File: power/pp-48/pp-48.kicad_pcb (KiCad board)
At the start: 4 copper layers, 106 x 72 mm, 218 parts, among them J1 XT90PW-M, J101 NODE 19V, J102 FRONT PANEL, J103 AUX, J2 CTRL IN, J201 NODE 19V, J202 FRONT PANEL, J203 AUX, J3 CTRL OUT, J4 12V AUX OUT, J5 SWD, Q1 2N7002, Q101 BSC070N10NS5, Q102 2N7002, Q103 2N7002, Q104 2N7002, Q105 2N7002, Q106 2N7002, Q107 2N7002, Q108 2N7002, Q109 2N7002, Q2 BSC040N10NS5, Q201 BSC070N10NS5, Q202 2N7002, Q203 2N7002, Q204 2N7002, Q205 2N7002, Q206 2N7002, Q207 2N7002, Q208 2N7002, Q209 2N7002, Q3 BSC040N10NS5, Q4 2N7002, Q6 2N7002, U1 LM5164DDA, U101 LM5069MM-2, U102 INA238AIDGSR, U103 74LVC1G74, U104 ADC121C027CIMK, U105 TCA9535PWR, U106 TLP176AM, U107 TLP176AM, U108 TLP291, U110 74LVC1G74, U2 URB4812YMD-6WR3, U201 LM5069MM-2, U202 INA238AIDGSR, U203 74LVC1G74, U204 ADC121C027CIMK, U205 TCA9535PWR, U206 TLP176AM, U207 TLP176AM, U208 TLP291, U210 74LVC1G74, U3 STM32G070CBT6, U4 ISO1640BD, U5 ISO7721D, U6 TCA9548APWR, U7 LM5069MM-1, U8 INA238AIDGSR, Y1 8MHz

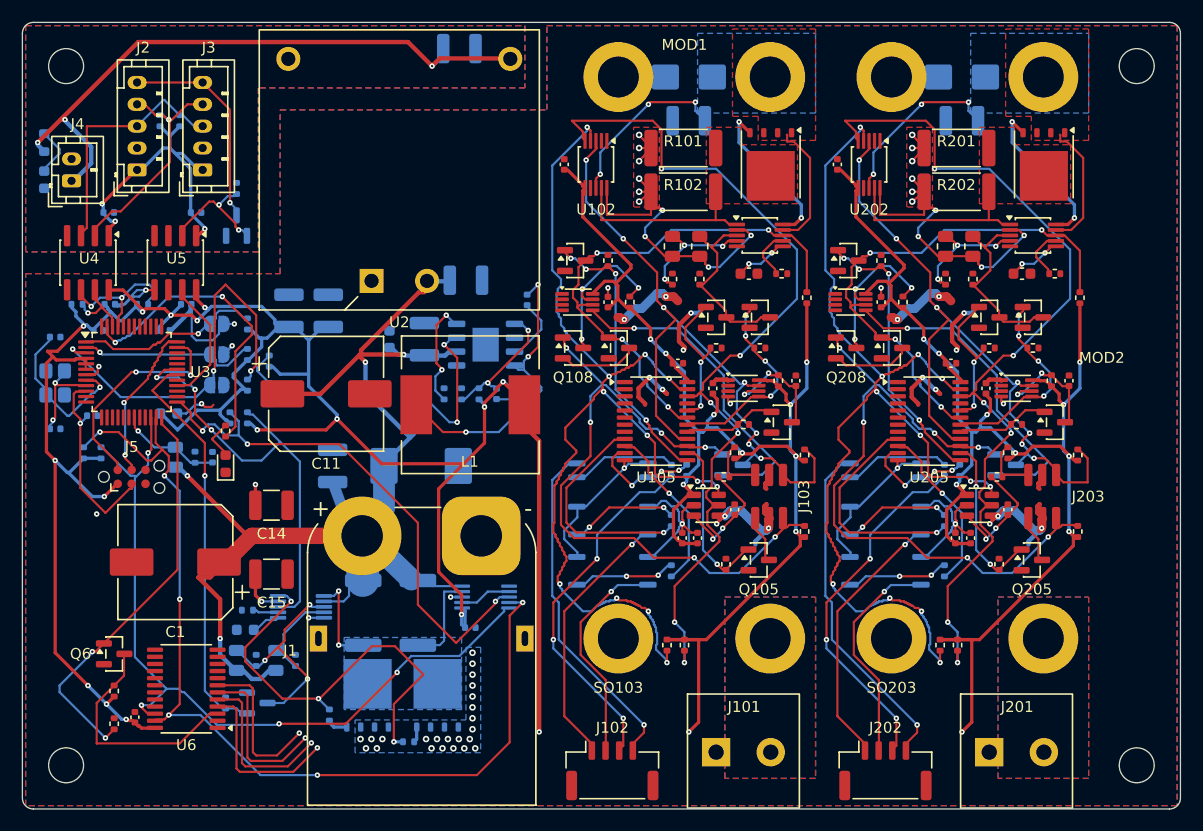
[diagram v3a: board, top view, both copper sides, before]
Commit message: pp-48: board routed as 2-slot units (N = 2, 106 x 72): DRC 0 unconnected / 0 parity / 0 errors (3 silk warnings, core D1); expander U5 in slot B, slot A's 11 lines on an In2 bus between via ladders (pad-via footprints, KRT routes only to pads), In2 no-via band and F rule areas over the SENSE pours (KRT ignores both), U10 PGD escape, J3 GND pins joined, 4 vias in U5's exposed pad; place.py slot table for both slots + unit parts, photoMOS stack 0.6 mm lower; route_hand.py channel / trunk / fences per unit (incl. last unit edge); netsplit.py per unit + slot A expander nets split at the bus; copycol.py unit pitch 50; expander ports reordered to the bus ladder; ADR 0004 decision 9 layout note; handoff
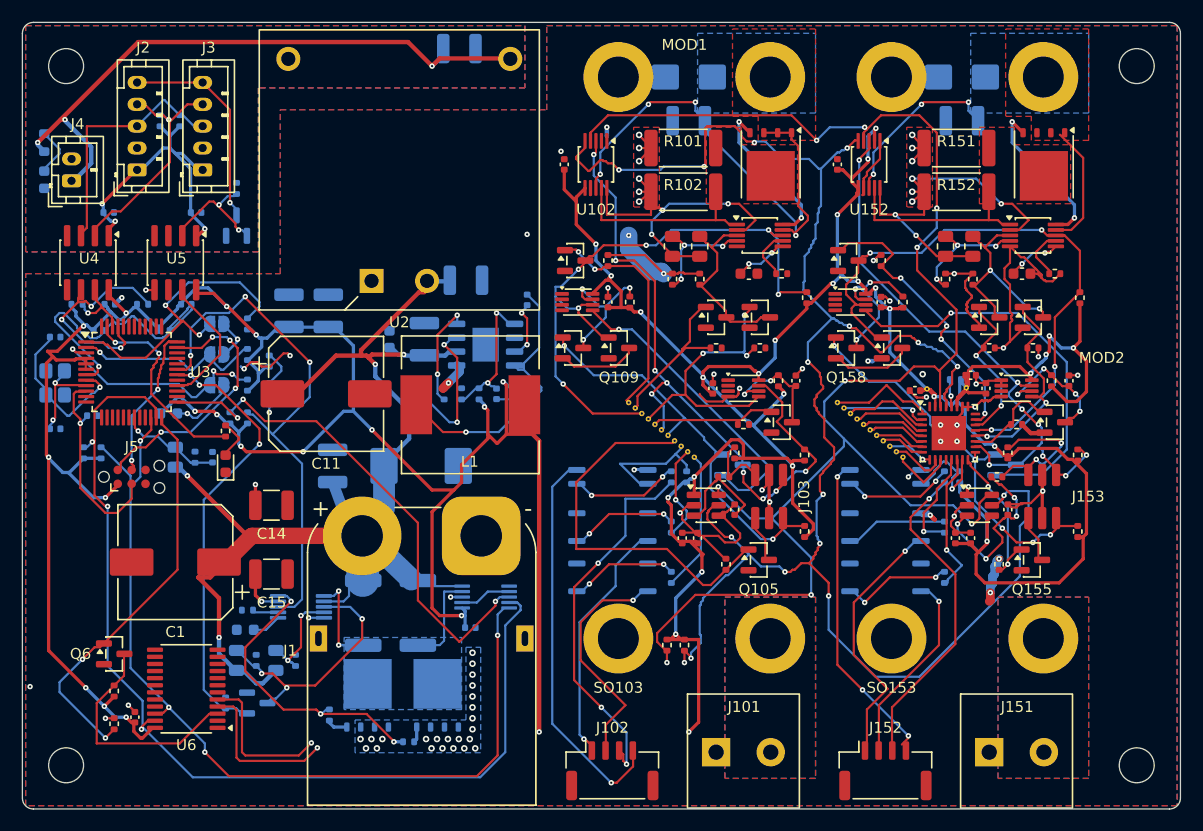
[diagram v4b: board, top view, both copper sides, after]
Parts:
- removed C201: 220n, Capacitor_SMD:C_0603_1608Metric
- removed C202: 2.2u 100V, Capacitor_SMD:C_1210_3225Metric
- removed C203, C204, C205, C206, C209, C210, C212: 100n, Capacitor_SMD:C_0402_1005Metric
- removed C211: 1u, Capacitor_SMD:C_0402_1005Metric
- removed D201: SMBJ60A, Diode_SMD:D_SMB
- removed J201: NODE 19V, pp48:TerminalBlock_Degson_DG128-5.0-02P
- removed J202: FRONT PANEL, Connector_JST:JST_GH_SM04B-GHS-TB_1x04-1MP_P1.25mm_Horizontal
- removed J203: AUX, pp48:PM_Aux_Socket_2x03_P1.27
- removed Q201: BSC070N10NS5, Package_TO_SOT_SMD:TDSON-8-1
- removed Q202, Q203, Q204, Q205, Q206, Q207, Q208, Q209: 2N7002, Package_TO_SOT_SMD:SOT-23
- removed R201, R202: 7m 2W, Resistor_SMD:R_2512_6332Metric
- removed R203: 143k, Resistor_SMD:R_0805_2012Metric
- removed R204, R208, R213, R214, R215: 10k, Resistor_SMD:R_0402_1005Metric
- removed R205: 124k, Resistor_SMD:R_0805_2012Metric
- removed R206: 4.99k, Resistor_SMD:R_0402_1005Metric
- removed R207: 13.7k, Resistor_SMD:R_0402_1005Metric
- removed R209, R210, R211, R212, R223, R228, R229: 100k, Resistor_SMD:R_0402_1005Metric
- removed R219, R220: 270, Resistor_SMD:R_0402_1005Metric
- removed R221: 220, Resistor_SMD:R_0402_1005Metric
- removed R222: 47k, Resistor_SMD:R_0402_1005Metric
- removed R224: 1k, Resistor_SMD:R_0402_1005Metric
- removed R226, R227: 4.7k, Resistor_SMD:R_0402_1005Metric
- removed SO201: S1 VIN, pp48:PM_Standoff_M2x7_SMTSO
- removed SO202: S2 GND, pp48:PM_Standoff_M2x7_SMTSO
- removed SO203: S3 GND, pp48:PM_Standoff_M2x7_SMTSO
- removed SO204: S4 VOUT, pp48:PM_Standoff_M2x7_SMTSO
- removed U201: LM5069MM-2, Package_SO:MSOP-10_3x3mm_P0.5mm
- removed U202: INA238AIDGSR, Package_SO:TSSOP-10_3x3mm_P0.5mm
- removed U203, U210: 74LVC1G74, Package_SO:VSSOP-8_2.3x2mm_P0.5mm
- removed U204: ADC121C027CIMK, Package_TO_SOT_SMD:TSOT-23-6
- removed U205: TCA9535PWR, Package_SO:TSSOP-24_4.4x7.8mm_P0.65mm
- removed U206, U207: TLP176AM, Package_SO:SOIC-4_4.55x3.7mm_P2.54mm
- removed U208: TLP291, Package_SO:SOIC-4_4.55x2.6mm_P1.27mm
- added BV100: , , F.Cu at (107.5, 134.8)
- added BV101: , , F.Cu at (108.1, 135.3)
- added BV102: , , F.Cu at (108.7, 135.8)
- added BV103: , , F.Cu at (109.3, 136.3)
- added BV104: , , F.Cu at (109.9, 136.8)
- added BV105: , , F.Cu at (110.5, 137.3)
- added BV106: , , F.Cu at (111.1, 137.8)
- added BV107: , , F.Cu at (111.7, 138.3)
- added BV108: , , F.Cu at (112.3, 138.8)
- added BV109: , , F.Cu at (112.9, 139.3)
- added BV110: , , F.Cu at (113.5, 139.8)
- added BV150: , , F.Cu at (126.6, 134.8)
- added BV151: , , F.Cu at (127.2, 135.3)
- added BV152: , , F.Cu at (127.8, 135.8)
- added BV153: , , F.Cu at (128.4, 136.3)
- added BV154: , , F.Cu at (129.0, 136.8)
- added BV155: , , F.Cu at (129.6, 137.3)
- added BV156: , , F.Cu at (130.2, 137.8)
- added BV157: , , F.Cu at (130.8, 138.3)
- added BV158: , , F.Cu at (131.4, 138.8)
- added BV159: , , F.Cu at (132.0, 139.3)
- added BV160: , , F.Cu at (132.6, 139.8)
- added C113: 100n, Capacitor_SMD:C_0402_1005Metric, F.Cu at (133.7, 133.7)
- added C151: 220n, Capacitor_SMD:C_0603_1608Metric, F.Cu at (143.5, 123.0)
- added C152: 2.2u 100V, Capacitor_SMD:C_1210_3225Metric, B.Cu at (138.0, 109.0)
- added C153: 100n, Capacitor_SMD:C_0402_1005Metric, F.Cu at (126.6, 113.0)
- added C154: 100n, Capacitor_SMD:C_0402_1005Metric, F.Cu at (140.2, 133.5)
- added C155: 100n, Capacitor_SMD:C_0402_1005Metric, F.Cu at (147.8, 132.8)
- added C156: 100n, Capacitor_SMD:C_0402_1005Metric, F.Cu at (142.2, 144.6)
- added C160: 100n, Capacitor_SMD:C_0402_1005Metric, F.Cu at (137.4, 147.2)
- added C161: 1u, Capacitor_SMD:C_0402_1005Metric, F.Cu at (138.8, 147.2)
- added C162: 100n, Capacitor_SMD:C_0402_1005Metric, F.Cu at (130.6, 125.6)
- added D151: SMBJ60A, Diode_SMD:D_SMB, B.Cu at (138.0, 105.0)
- added J151: NODE 19V, pp48:TerminalBlock_Degson_DG128-5.0-02P, F.Cu at (140.5, 166.8)
- added J152: FRONT PANEL, Connector_JST:JST_GH_SM04B-GHS-TB_1x04-1MP_P1.25mm_Horizontal, F.Cu at (131.0, 168.5)
- added J153: AUX, pp48:PM_Aux_Socket_2x03_P1.27, F.Cu at (145.3, 143.4)
- added PV1B3: , , F.Cu at (134.8, 133.6)
- added PV1B4: , , F.Cu at (138.4, 133.4)
- added Q151: BSC070N10NS5, Package_TO_SOT_SMD:TDSON-8-1, F.Cu at (145.5, 113.0)
- added Q152: 2N7002, Package_TO_SOT_SMD:SOT-23, F.Cu at (140.5, 127.0)
- added Q153: 2N7002, Package_TO_SOT_SMD:SOT-23, F.Cu at (144.5, 127.0)
- added Q154: 2N7002, Package_TO_SOT_SMD:SOT-23, F.Cu at (146.5, 136.6)
- added Q155: 2N7002, Package_TO_SOT_SMD:SOT-23, F.Cu at (144.4, 149.2)
- added Q156: 2N7002, Package_TO_SOT_SMD:SOT-23, B.Cu at (142.0, 140.5)
- added Q157: 2N7002, Package_TO_SOT_SMD:SOT-23, F.Cu at (127.6, 121.8)
- added Q158: 2N7002, Package_TO_SOT_SMD:SOT-23, F.Cu at (127.4, 129.8)
- added Q159: 2N7002, Package_TO_SOT_SMD:SOT-23, F.Cu at (131.6, 129.8)
- added R130: 10k, Resistor_SMD:R_0402_1005Metric, B.Cu at (137.4, 132.7)
- added R151: 7m 2W, Resistor_SMD:R_2512_6332Metric, F.Cu at (137.5, 111.5)
- added R152: 7m 2W, Resistor_SMD:R_2512_6332Metric, F.Cu at (137.5, 115.5)
- added R153: 143k, Resistor_SMD:R_0805_2012Metric, F.Cu at (139.0, 120.5)
- added R154: 10k, Resistor_SMD:R_0402_1005Metric, F.Cu at (139.0, 123.5)
- added R155: 124k, Resistor_SMD:R_0805_2012Metric, F.Cu at (136.5, 120.5)
- added R156: 4.99k, Resistor_SMD:R_0402_1005Metric, F.Cu at (136.5, 123.5)
- added R157: 13.7k, Resistor_SMD:R_0402_1005Metric, F.Cu at (146.5, 123.0)
- added R158: 10k, Resistor_SMD:R_0402_1005Metric, F.Cu at (148.8, 125.2)
- added R159: 100k, Resistor_SMD:R_0402_1005Metric, F.Cu at (140.5, 129.8)
- added R160: 100k, Resistor_SMD:R_0402_1005Metric, F.Cu at (144.5, 129.8)
- added R161: 100k, Resistor_SMD:R_0402_1005Metric, F.Cu at (146.2, 132.8)
- added R162: 100k, Resistor_SMD:R_0402_1005Metric, F.Cu at (143.0, 136.8)
- added R163: 10k, Resistor_SMD:R_0402_1005Metric, F.Cu at (148.6, 139.6)
- added R164: 10k, Resistor_SMD:R_0402_1005Metric, F.Cu at (148.6, 146.6)
- added R165: 10k, Resistor_SMD:R_0402_1005Metric, F.Cu at (142.2, 139.4)
- added R169: 270, Resistor_SMD:R_0402_1005Metric, B.Cu at (136.4, 146.2)
- added R170: 270, Resistor_SMD:R_0402_1005Metric, B.Cu at (136.4, 150.8)
- added R171: 220, Resistor_SMD:R_0402_1005Metric, B.Cu at (136.4, 141.6)
- added R172: 47k, Resistor_SMD:R_0402_1005Metric, B.Cu at (137.8, 141.6)
- added R173: 100k, Resistor_SMD:R_0402_1005Metric, F.Cu at (141.4, 149.6)
- added R174: 1k, Resistor_SMD:R_0402_1005Metric, F.Cu at (141.2, 141.6)
- added R178: 100k, Resistor_SMD:R_0402_1005Metric, F.Cu at (132.6, 125.6)
- added R179: 100k, Resistor_SMD:R_0402_1005Metric, F.Cu at (130.6, 121.8)
- added SO151: S1 VIN, pp48:PM_Standoff_M2x7_SMTSO, F.Cu at (145.4, 105.0)
- added SO152: S2 GND, pp48:PM_Standoff_M2x7_SMTSO, F.Cu at (131.6, 105.0)
- added SO153: S3 GND, pp48:PM_Standoff_M2x7_SMTSO, F.Cu at (131.6, 156.4)
- added SO154: S4 VOUT, pp48:PM_Standoff_M2x7_SMTSO, F.Cu at (145.4, 156.4)
- added U151: LM5069MM-2, Package_SO:MSOP-10_3x3mm_P0.5mm, F.Cu at (144.5, 119.5)
- added U152: INA238AIDGSR, Package_SO:TSSOP-10_3x3mm_P0.5mm, F.Cu at (129.5, 113.0)
- added U153: 74LVC1G74, Package_SO:VSSOP-8_2.3x2mm_P0.5mm, F.Cu at (143.0, 133.5)
- added U154: ADC121C027CIMK, Package_TO_SOT_SMD:TSOT-23-6, F.Cu at (139.6, 144.2)
- added U156: TLP176AM, Package_SO:SOIC-4_4.55x3.7mm_P2.54mm, B.Cu at (131.0, 146.2)
- added U157: TLP176AM, Package_SO:SOIC-4_4.55x3.7mm_P2.54mm, B.Cu at (131.0, 150.8)
- added U158: TLP291, Package_SO:SOIC-4_4.55x2.6mm_P1.27mm, B.Cu at (131.0, 141.6)
- added U160: 74LVC1G74, Package_SO:VSSOP-8_2.3x2mm_P0.5mm, F.Cu at (127.8, 125.6)
- U105: value TCA9535PWR -> TCA6424ARGJR; footprint Package_SO:TSSOP-24_4.4x7.8mm_P0.65mm -> Package_DFN_QFN:VQFN-32-1EP_5x5mm_P0.5mm_EP3.15x3.15mm
- moved C109 26.8 mm to (138.8, 132.3)
- moved U105 26.8 mm to (136.8, 137.6)
- moved R120 0.60 mm to (111.4, 150.8)
- moved U107 0.60 mm to (106.0, 150.8)
- moved R119 0.60 mm to (111.4, 146.2)
- moved R121 0.60 mm to (111.4, 141.6)
- moved R122 0.60 mm to (112.8, 141.6)
- moved U106 0.60 mm to (106.0, 146.2)
- moved U108 0.60 mm to (106.0, 141.6)
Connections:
- net /Column 1/ARM renamed /Unit 1/A_ARM
- net /Column 1/ARMS_M renamed /Unit 1/A_ARMS_M
- net /Column 1/ARMS_N renamed /Unit 1/A_ARMS_N
- net /Column 1/CLRN renamed /Unit 1/A_CLRN
- net /Column 1/GATE renamed /Unit 1/A_GATE
- net /Column 1/ID renamed /Unit 1/A_ID
- net /Column 1/ID_F renamed /Unit 1/A_ID_F
- net /Column 1/NODE renamed /Unit 1/A_NODE
- net /Column 1/OUT renamed /Unit 1/A_OUT
- net /Column 1/OVLO renamed /Unit 1/A_OVLO
- net /Column 1/PLED_A renamed /Unit 1/A_PLED_A
- net /Column 1/PLED_N renamed /Unit 1/A_PLED_N
- net /Column 1/PLED_P renamed /Unit 1/A_PLED_P
- net /Column 1/PWR renamed /Unit 1/A_PWR
- net /Column 1/PWRD_A renamed /Unit 1/A_PWRD_A
- net /Column 1/PWR_SW renamed /Unit 1/A_PWR_SW
- net /Column 1/RSTD_A renamed /Unit 1/A_RSTD_A
- net /Column 1/RST_SW renamed /Unit 1/A_RST_SW
- net /Column 1/RUN renamed /Unit 1/A_RUN
- net /Column 1/SENSE renamed /Unit 1/A_SENSE
- net /Column 1/TIMER renamed /Unit 1/A_TIMER
- net /Column 1/UVLO renamed /Unit 1/A_UVLO
- J103 pad 1: /Column 1/OVK -> /Unit 1/A_OVK
- J103 pad 2: /Column 1/PG -> /Unit 1/A_PG
- Q102 pad 1: /Column 1/OFF -> /Unit 1/A_OFF
- Q103 pad 1: /Column 1/LQ -> /Unit 1/A_LQ
- Q104 pad 1: /Column 1/LCLR -> /Unit 1/A_LCLR
- Q105 pad 1: /Column 1/RUNOFF -> /Unit 1/A_RUNOFF
- Q106 pad 2: /Column 1/PG -> /Unit 1/A_PG
- Q106 pad 3: /Column 1/OVK -> /Unit 1/A_OVK
- Q107 pad 1: /Column 1/DISARM -> /Unit 1/A_DISARM
- Q107 pad 3: /Column 1/PGD -> /Unit 1/A_PGD
- Q108 pad 1: /Column 1/PG -> /Unit 1/A_PG
- Q109 pad 1: /Column 1/PGD -> /Unit 1/A_PGD
- R108 pad 2: /Column 1/PGD -> /Unit 1/A_PGD
- R109 pad 1: /Column 1/OFF -> /Unit 1/A_OFF
- R110 pad 1: /Column 1/LQ -> /Unit 1/A_LQ
- R112 pad 1: /Column 1/LCLR -> /Unit 1/A_LCLR
- R113 pad 2: /Column 1/OVK -> /Unit 1/A_OVK
- R114 pad 2: /Column 1/PG -> /Unit 1/A_PG
- R119 pad 1: /Column 1/PWRD -> /Unit 1/A_PWRD
- R120 pad 1: /Column 1/RSTD -> /Unit 1/A_RSTD
- R122 pad 2: /Column 1/LED -> /Unit 1/A_LED
- R123 pad 1: /Column 1/RUNOFF -> /Unit 1/A_RUNOFF
- R126 pad 2: /COL1_SDA -> /UNIT1_SDA
- R127 pad 2: /COL1_SCL -> /UNIT1_SCL
- R129 pad 1: /Column 1/DISARM -> /Unit 1/A_DISARM
- U101 pad 8: /Column 1/PGD -> /Unit 1/A_PGD
- U102 pad 3: /Column 1/OVK -> /Unit 1/A_OVK
- U102 pad 4: /COL1_SDA -> /UNIT1_SDA
- U102 pad 5: /COL1_SCL -> /UNIT1_SCL
- U103 pad 5: /Column 1/LQ -> /Unit 1/A_LQ
- U103 pad 7: /Column 1/OVK -> /Unit 1/A_OVK
- U104 pad 5: /COL1_SCL -> /UNIT1_SCL
- U104 pad 6: /COL1_SDA -> /UNIT1_SDA
- U105 pad 1: unconnected-(U105-~{INT}-Pad1) -> /Unit 1/A_DISARM
- U105 pad 10: /Column 1/RSTD -> /Unit 1/A_PWRD
- U105 pad 11: /Column 1/LED -> /Unit 1/A_RSTD
- U105 pad 12: GND -> unconnected-(U105-P13-Pad12)
- U105 pad 13: /Column 1/DISARM -> /Unit 1/B_PWRD
- U105 pad 14: /Column 1/RUNOFF -> /Unit 1/B_RSTD
- U105 pad 15: /Column 1/PG -> /Unit 1/B_LED
- U105 pad 16: /Column 1/OVK -> /Unit 1/B_RUNOFF
- U105 pad 17: /Column 1/LCLR -> /Unit 1/B_PG
- U105 pad 18: /Column 1/LQ -> /Unit 1/B_OVK
- U105 pad 19: /Column 1/PGD -> /Unit 1/B_LCLR
- U105 pad 2: GND -> /Unit 1/A_OFF
- U105 pad 20: /Column 1/OFF -> /Unit 1/B_LQ
- U105 pad 21: GND -> /Unit 1/B_PGD
- U105 pad 22: /COL1_SCL -> /Unit 1/B_OFF
- U105 pad 23: /COL1_SDA -> /Unit 1/B_DISARM
- U105 pad 24: +3V3 -> unconnected-(U105-P27-Pad24)
- U105 pad 3: GND -> /Unit 1/A_PGD
- U105 pad 4: unconnected-(U105-P00-Pad4) -> /Unit 1/A_LQ
- U105 pad 5: unconnected-(U105-P01-Pad5) -> /Unit 1/A_LCLR
- U105 pad 6: unconnected-(U105-P02-Pad6) -> /Unit 1/A_OVK
- U105 pad 7: unconnected-(U105-P03-Pad7) -> /Unit 1/A_PG
- U105 pad 8: unconnected-(U105-P04-Pad8) -> /Unit 1/A_RUNOFF
- U105 pad 9: /Column 1/PWRD -> /Unit 1/A_LED
- U108 pad 4: /Column 1/LED -> /Unit 1/A_LED
- U110 pad 6: /Column 1/PGD -> /Unit 1/A_PGD
- U6 pad 4: /COL1_SDA -> /UNIT1_SDA
- U6 pad 5: /COL1_SCL -> /UNIT1_SCL
- U6 pad 6: /COL2_SDA -> unconnected-(U6-SD1-Pad6)
- U6 pad 7: /COL2_SCL -> unconnected-(U6-SC1-Pad7)
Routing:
- net /UNIT1_SCL: track 0.00 -> 220.8 mm, vias 0 -> 17
- net /UNIT1_SDA: track 0.00 -> 198.2 mm, vias 0 -> 10
- net /COL2_SDA: track 177.0 -> 0.00 mm, vias 13 -> 0
- net /COL2_SCL: track 166.2 -> 0.00 mm, vias 7 -> 0
- net /COL1_SDA: track 150.0 -> 0.00 mm, vias 13 -> 0
- net /COL1_SCL: track 139.2 -> 0.00 mm, vias 7 -> 0
- net /Unit 1/A_OVK: track 0.00 -> 86.6 mm, vias 0 -> 9
- net /Unit 1/A_PGD: track 0.00 -> 84.1 mm, vias 0 -> 6
- net /Column 2/OVK: track 63.3 -> 0.00 mm, vias 7 -> 0
- net /Column 1/OVK: track 63.3 -> 0.00 mm, vias 7 -> 0
- net /Unit 1/A_PG: track 0.00 -> 59.3 mm, vias 0 -> 2
- net /Column 2/PG: track 59.0 -> 0.00 mm, vias 6 -> 0
- net /Column 1/PG: track 59.0 -> 0.00 mm, vias 6 -> 0
- net /Unit 1/A_RUNOFF: track 0.00 -> 57.8 mm
- net /Unit 1/B_PGD: track 0.00 -> 53.9 mm, vias 0 -> 4
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- added copper zone on B.Cu, net /Unit 1/B_NODE
- added copper zone on F.Cu, net /Unit 1/B_NODE
- added copper zone on B.Cu, net /Unit 1/B_OUT
- added copper zone on F.Cu, net /Unit 1/B_OUT
- added copper zone on F.Cu, net /Unit 1/B_SENSE
- removed copper zone on B.Cu, net /Column 2/NODE
- removed copper zone on F.Cu, net /Column 2/NODE
- removed copper zone on B.Cu, net /Column 2/OUT
- removed copper zone on F.Cu, net /Column 2/OUT
- removed copper zone on F.Cu, net /Column 2/SENSE
